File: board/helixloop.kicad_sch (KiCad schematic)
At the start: 69 parts, among them J6 USB_C_Receptacle, J7 Conn_01x03_Pin, SW6 SW_Push, U10 QSPI Flash, U6 USBLC6-2P6, U7 RP2040, U9 RT9078, Y6 12MHz

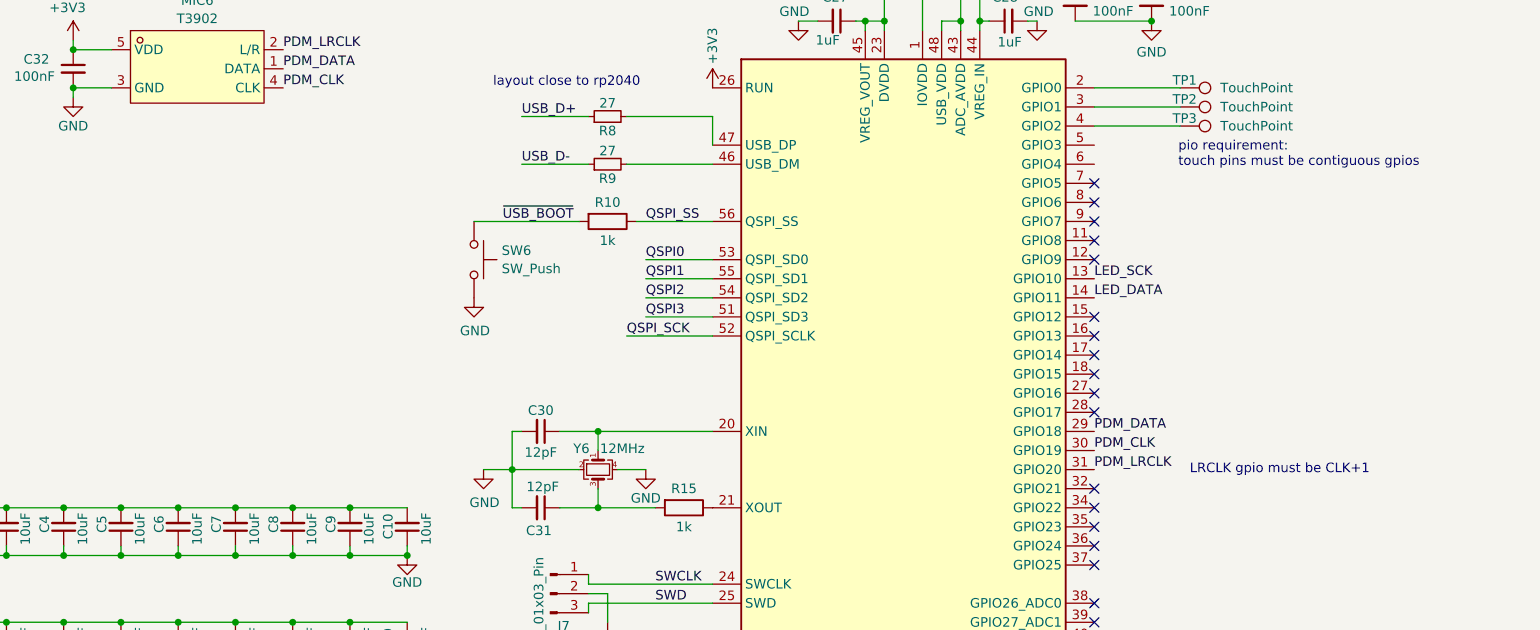
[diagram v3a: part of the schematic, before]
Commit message: add 3 touch points
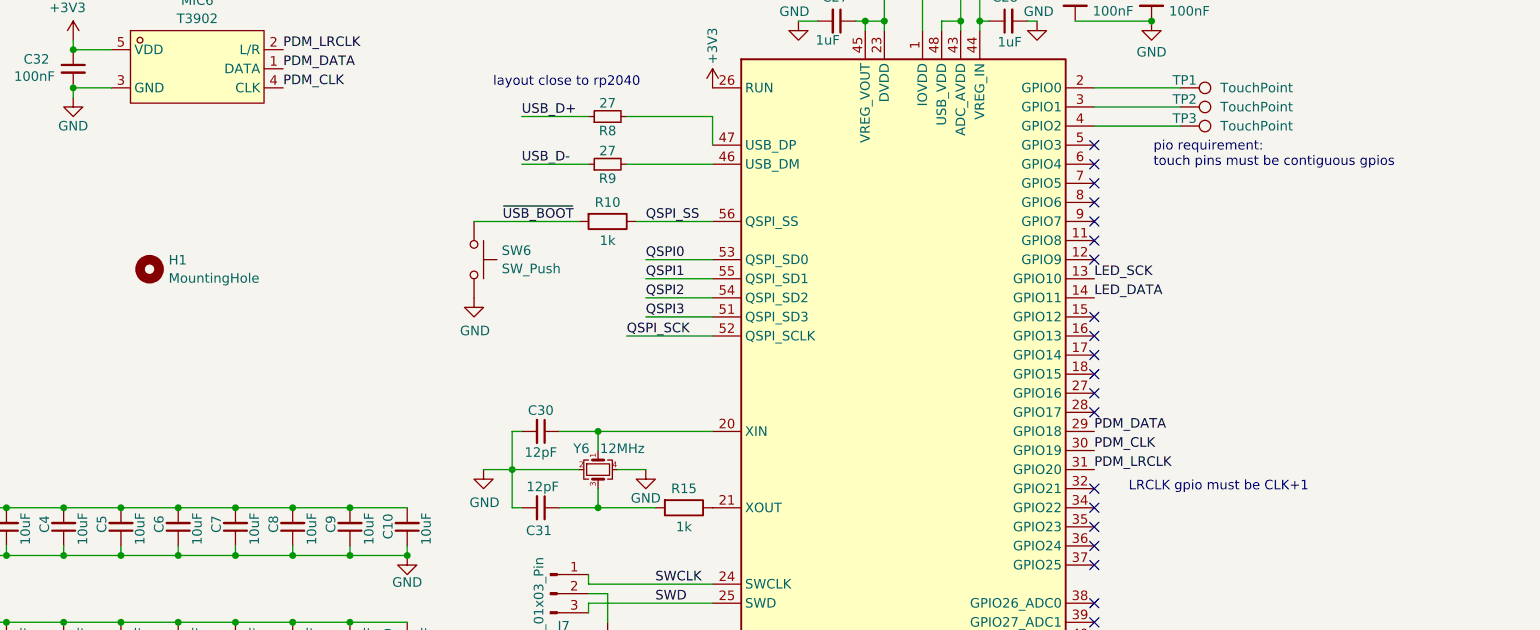
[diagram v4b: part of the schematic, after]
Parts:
- added H1: MountingHole, MountingHole:MountingHole_2.5mm, symbol Mechanical:MountingHole
- TP1: renamed from TP3; footprint TestPoint:TestPoint_Pad_D2.5mm -> helixloop:TouchPoint
- TP2: renamed from TP1; footprint TestPoint:TestPoint_Pad_D2.5mm -> helixloop:TouchPoint
- TP3: renamed from TP2; footprint TestPoint:TestPoint_Pad_D2.5mm -> helixloop:TouchPoint
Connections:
- net at TP1.1: now also U7.2 (GPIO0); no longer U7.4 (GPIO2)
- net at TP2.1: now also U7.3 (GPIO1); no longer U7.2 (GPIO0)
- net at TP3.1: now also U7.4 (GPIO2); no longer U7.3 (GPIO1)
- no-connect marks 32 -> 34
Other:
- moved on the sheet: TP1, TP2, TP3
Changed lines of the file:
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@@
 	)
 	(no_connect
+		(at 224.79 54.61)
+	)
+	(no_connect
 		(at 43.18 68.58)
 	)
@@
 	)
 	(no_connect
+		(at 224.79 52.07)
+	)
+	(no_connect
 		(at 224.79 77.47)
 	)
@@
 	(text "pio requirement:\ntouch pins must be contiguous gpios"
 		(exclude_from_sim no)
-		(at 235.966 53.34 0)
+		(at 232.664 53.34 0)
 		(effects
 			(font
@@
 	(text "LRCLK gpio must be CLK+1"
 		(exclude_from_sim no)
-		(at 237.49 95.25 0)
+		(at 229.362 97.536 0)
 		(effects
 			(font
@@
 	)
 	(symbol
+		(lib_id "Mechanical:MountingHole")
+		(at 99.06 68.58 0)
+		(unit 1)
+		(exclude_from_sim yes)
+		(in_bom no)
+		(on_board yes)
+		(dnp no)
+		(fields_autoplaced yes)
+		(property "Reference" "H1"
+			(at 101.6 67.3678 0)
+			(effects
+				(font
+					(size 1.27 1.27)
+				)
+				(justify left)
+			)
+		)
+		(property "Value" "MountingHole"
+			(at 101.6 69.7921 0)
+			(effects
+				(font
+					(size 1.27 1.27)
+				)
+				(justify left)
+			)
+		)
+		(property "Footprint" "MountingHole:MountingHole_2.5mm"
+			(at 99.06 68.58 0)
+			(effects
+				(font
+					(size 1.27 1.27)
+				)
+				(hide yes)
+			)
+		)
+		(property "Datasheet" "~"
+			(at 99.06 68.58 0)
+			(effects
+				(font
+					(size 1.27 1.27)
+				)
+				(hide yes)
+			)
+		)
+		(property "Description" "Mounting Hole without connection"
+			(at 99.06 68.58 0)
+			(effects
+				(font
+					(size 1.27 1.27)
+				)
+				(hide yes)
+			)
+		)
+		(property "Designation" ""
+			(at 99.06 68.58 0)
+			(effects
+				(font
+					(size 1.27 1.27)
+				)
+				(hide yes)
+			)
+		)
+		(instances
+			(project ""
+				(path "/1f30b1ea-44f0-467a-8ed8-643be513058b"
+					(reference "H1")
+					(unit 1)
+				)
+			)
+		)
+	)
+	(symbol
 		(lib_id "helixloop:QSPI Flash")
 		(at 241.3 152.4 0)
@@
 	(symbol
 		(lib_id "Connector:TestPoint")
-		(at 236.22 49.53 270)
+		(at 236.22 44.45 270)
 		(unit 1)
 		(exclude_from_sim no)
@@
 		(on_board yes)
 		(dnp no)
-		(property "Reference" "TP3"
-			(at 235.204 48.514 90)
+		(property "Reference" "TP1"
+			(at 235.204 43.434 90)
 			(effects
 				(font
@@
 		)
 		(property "Value" "TouchPoint"
-			(at 241.554 49.53 90)
+			(at 241.554 44.45 90)
 			(effects
 				(font
@@
 			)
 		)
-		(property "Footprint" "TestPoint:TestPoint_Pad_D2.5mm"
-			(at 236.22 54.61 0)
+		(property "Footprint" "helixloop:TouchPoint"
+			(at 236.22 49.53 0)
 			(effects
 				(font
@@
 		)
 		(property "Datasheet" "~"
-			(at 236.22 54.61 0)
+			(at 236.22 49.53 0)
 			(effects
 				(font
@@
 		)
 		(property "Description" "test point"
-			(at 236.22 49.53 0)
+			(at 236.22 44.45 0)
 			(effects
 				(font
@@
 		)
 		(property "Designation" ""
-			(at 236.22 49.53 0)
+			(at 236.22 44.45 0)
 			(effects
 				(font
@@
 			(project "helixloop"
 				(path "/1f30b1ea-44f0-467a-8ed8-643be513058b"
-					(reference "TP3")
+					(reference "TP1")
 					(unit 1)
 				)
@@
 	(symbol
 		(lib_id "Connector:TestPoint")
-		(at 236.22 46.99 270)
+		(at 236.22 49.53 270)
 		(unit 1)
 		(exclude_from_sim no)
@@
 		(on_board yes)
 		(dnp no)
-		(property "Reference" "TP2"
-			(at 235.204 45.974 90)
+		(property "Reference" "TP3"
+			(at 235.204 48.514 90)
 			(effects
 				(font
@@
 		)
 		(property "Value" "TouchPoint"
-			(at 241.554 46.99 90)
+			(at 241.554 49.53 90)
 			(effects
 				(font
@@
 			)
 		)
-		(property "Footprint" "TestPoint:TestPoint_Pad_D2.5mm"
-			(at 236.22 52.07 0)
+		(property "Footprint" "helixloop:TouchPoint"
+			(at 236.22 54.61 0)
 			(effects
 				(font
@@
 		)
 		(property "Datasheet" "~"
-			(at 236.22 52.07 0)
+			(at 236.22 54.61 0)
 			(effects
 				(font
@@
 		)
 		(property "Description" "test point"
-			(at 236.22 46.99 0)
+			(at 236.22 49.53 0)
 			(effects
 				(font
@@
 		)
 		(property "Designation" ""
-			(at 236.22 46.99 0)
+			(at 236.22 49.53 0)
 			(effects
 				(font
@@
 			(project "helixloop"
 				(path "/1f30b1ea-44f0-467a-8ed8-643be513058b"
-					(reference "TP2")
+					(reference "TP3")
 					(unit 1)
 				)
@@
 	(symbol
 		(lib_id "Connector:TestPoint")
-		(at 236.22 44.45 270)
+		(at 236.22 46.99 270)
 		(unit 1)
 		(exclude_from_sim no)
@@
 		(on_board yes)
 		(dnp no)
-		(property "Reference" "TP1"
-			(at 235.204 43.434 90)
+		(property "Reference" "TP2"
+			(at 235.204 45.974 90)
 			(effects
 				(font
@@
 		)
 		(property "Value" "TouchPoint"
-			(at 241.554 44.45 90)
+			(at 241.554 46.99 90)
 			(effects
 				(font
@@
 			)
 		)
-		(property "Footprint" "TestPoint:TestPoint_Pad_D2.5mm"
-			(at 236.22 49.53 0)
+		(property "Footprint" "helixloop:TouchPoint"
+			(at 236.22 52.07 0)
 			(effects
 				(font
@@
 		)
 		(property "Datasheet" "~"
-			(at 236.22 49.53 0)
+			(at 236.22 52.07 0)
 			(effects
 				(font
@@
 		)
 		(property "Description" "test point"
-			(at 236.22 44.45 0)
+			(at 236.22 46.99 0)
 			(effects
 				(font
@@
 		)
 		(property "Designation" ""
-			(at 236.22 44.45 0)
+			(at 236.22 46.99 0)
 			(effects
 				(font
@@
 			(project "helixloop"
 				(path "/1f30b1ea-44f0-467a-8ed8-643be513058b"
-					(reference "TP1")
+					(reference "TP2")
 					(unit 1)
 				)

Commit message: add spiral drawing back in and remove homedir path; fix mic symbol link
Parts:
- MIC6: footprint easyeda2kicad:MIC-SMD_5P-L3.5-W2.7-TL_MMICT390200012 -> helixloop:KEY-SMD_L3.0-W2.5-LS4.0
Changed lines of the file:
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@@
 			)
 		)
-		(property "Footprint" "easyeda2kicad:MIC-SMD_5P-L3.5-W2.7-TL_MMICT390200012"
+		(property "Footprint" "helixloop:KEY-SMD_L3.0-W2.5-LS4.0"
 			(at 105.156 51.816 0)
 			(effects

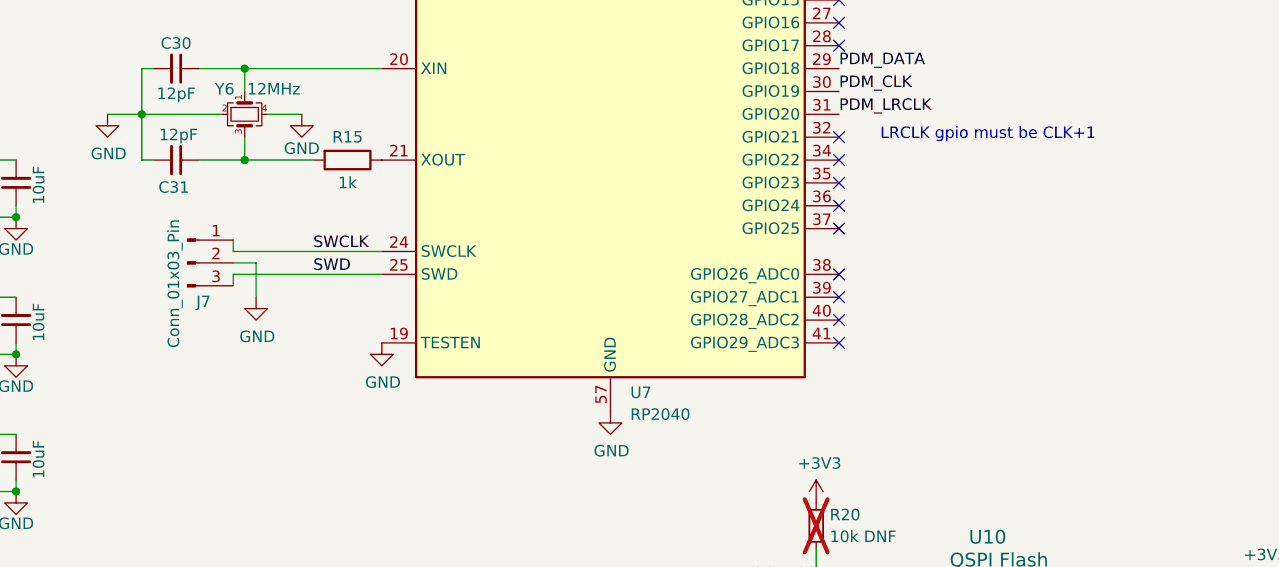
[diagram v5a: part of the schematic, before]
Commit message: export swd pins and all four analog pins to small tht connectors; tweak back-copper gnd fill margins
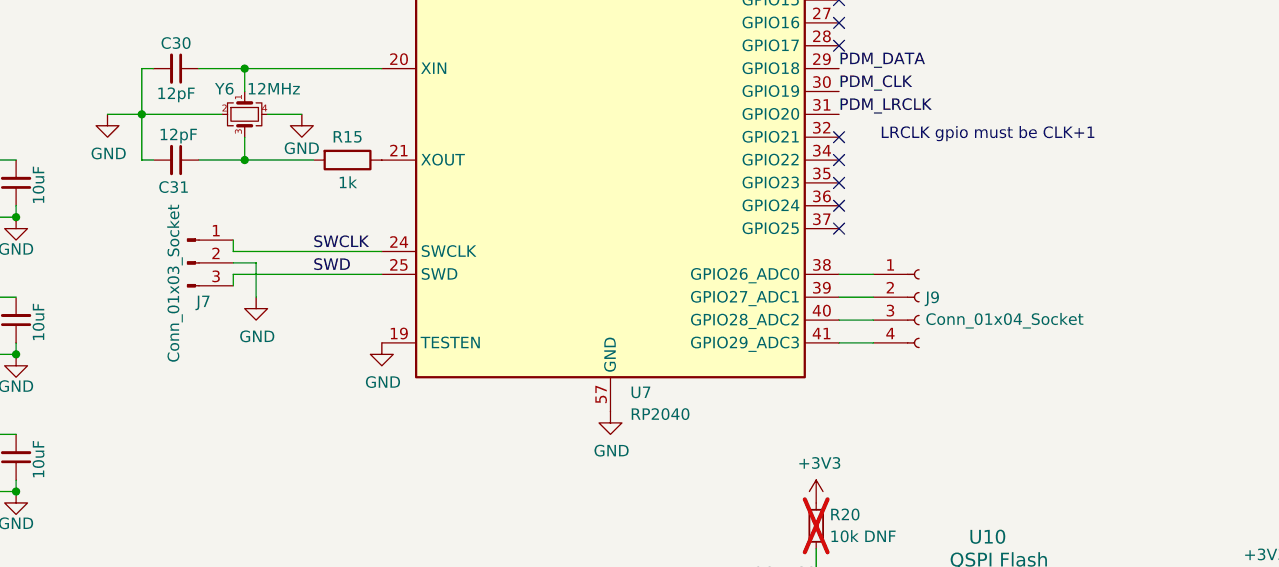
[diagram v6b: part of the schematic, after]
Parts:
- added J9: Conn_01x04_Socket, helixloop:MinimalPinSocket_1x04_P1.27mm_Vertical, symbol Connector:Conn_01x04_Socket
- J7: value Conn_01x03_Pin -> Conn_01x03_Socket; footprint penta:SMD_Pad_01x03_1.27mm -> helixloop:MinimalPinSocket_1x03_P1.27mm_Vertical
- MIC6: footprint helixloop:KEY-SMD_L3.0-W2.5-LS4.0 -> helixloop:MIC_T3902
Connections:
- net at U7.38 (GPIO26_ADC0): now also J9.1 (Pin_1)
- net at U7.39 (GPIO27_ADC1): now also J9.2 (Pin_2)
- net at U7.40 (GPIO28_ADC2): now also J9.3 (Pin_3)
- net at U7.41 (GPIO29_ADC3): now also J9.4 (Pin_4)
- no-connect marks 34 -> 30
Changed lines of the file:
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@@
 	)
 	(no_connect
-		(at 224.79 113.03)
-	)
-	(no_connect
 		(at 224.79 85.09)
 	)
@@
 	)
 	(no_connect
-		(at 224.79 120.65)
-	)
-	(no_connect
 		(at 224.79 97.79)
 	)
@@
 	)
 	(no_connect
-		(at 224.79 115.57)
-	)
-	(no_connect
 		(at 43.18 53.34)
 	)
@@
 	)
 	(no_connect
-		(at 224.79 118.11)
-	)
-	(no_connect
 		(at 224.79 67.31)
 	)
@@
 	(wire
 		(pts
+			(xy 224.79 118.11) (xy 228.6 118.11)
+		)
+		(stroke
+			(width 0)
+			(type default)
+		)
+	)
+	(wire
+		(pts
 			(xy 201.93 22.86) (xy 209.55 22.86)
 		)
@@
 	(wire
 		(pts
+			(xy 224.79 120.65) (xy 228.6 120.65)
+		)
+		(stroke
+			(width 0)
+			(type default)
+		)
+	)
+	(wire
+		(pts
 			(xy 133.35 106.68) (xy 133.35 105.41)
 		)
@@
 	(wire
 		(pts
+			(xy 224.79 113.03) (xy 228.6 113.03)
+		)
+		(stroke
+			(width 0)
+			(type default)
+		)
+	)
+	(wire
+		(pts
 			(xy 118.11 121.92) (xy 110.49 121.92)
 		)
@@
 	(wire
 		(pts
+			(xy 224.79 115.57) (xy 228.6 115.57)
+		)
+		(stroke
+			(width 0)
+			(type default)
+		)
+	)
+	(wire
+		(pts
 			(xy 74.93 168.91) (xy 77.47 168.91)
 		)
@@
 			)
 		)
-		(property "Footprint" "helixloop:KEY-SMD_L3.0-W2.5-LS4.0"
+		(property "Footprint" "helixloop:MIC_T3902"
 			(at 105.156 51.816 0)
 			(effects
@@
 			)
 		)
-		(property "Value" "Conn_01x03_Pin"
+		(property "Value" "Conn_01x03_Socket"
 			(at 150.876 114.046 90)
 			(effects
@@
 			)
 		)
-		(property "Footprint" "penta:SMD_Pad_01x03_1.27mm"
+		(property "Footprint" "helixloop:MinimalPinSocket_1x03_P1.27mm_Vertical"
 			(at 152.4 111.76 0)
 			(effects
@@
 					(unit 1)
 				)
+			)
+		)
+	)
+	(symbol
+		(lib_id "Connector:Conn_01x04_Socket")
+		(at 233.68 115.57 0)
+		(unit 1)
+		(exclude_from_sim no)
+		(in_bom no)
+		(on_board yes)
+		(dnp no)
+		(fields_autoplaced yes)
+		(property "Reference" "J9"
+			(at 234.3912 115.6278 0)
+			(effects
+				(font
+					(size 1.27 1.27)
+				)
+				(justify left)
+			)
+		)
+		(property "Value" "Conn_01x04_Socket"
+			(at 234.3912 118.0521 0)
+			(effects
+				(font
+					(size 1.27 1.27)
+				)
+				(justify left)
+			)
+		)
+		(property "Footprint" "helixloop:MinimalPinSocket_1x04_P1.27mm_Vertical"
+			(at 233.68 115.57 0)
+			(effects
+				(font
+					(size 1.27 1.27)
+				)
+				(hide yes)
+			)
+		)
+		(property "Datasheet" "~"
+			(at 233.68 115.57 0)
+			(effects
+				(font
+					(size 1.27 1.27)
+				)
+				(hide yes)
+			)
+		)
+		(property "Description" "Generic connector, single row, 01x04, script generated"
+			(at 233.68 115.57 0)
+			(effects
+				(font
+					(size 1.27 1.27)
+				)
+				(hide yes)
+			)
+		)
+		(property "Designation" ""
+			(at 233.68 115.57 0)
+			(effects
+				(font
+					(size 1.27 1.27)
+				)
+				(hide yes)
+			)
+		)
+		(pin "2"
+		)
+		(pin "4"
+		)
+		(pin "3"
+		)
+		(pin "1"
+		)
+		(instances
+			(project ""
+				(path "/1f30b1ea-44f0-467a-8ed8-643be513058b"
+					(reference "J9")
+					(unit 1)
+				)

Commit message: add more mounting holes
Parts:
- removed H1: MountingHole, MountingHole:MountingHole_2.5mm, symbol Mechanical:MountingHole
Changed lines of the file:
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@@
-	)
-	(symbol
-		(lib_id "Mechanical:MountingHole")
-		(at 99.06 68.58 0)
-		(unit 1)
-		(exclude_from_sim yes)
-		(in_bom no)
-		(on_board yes)
-		(dnp no)
-		(fields_autoplaced yes)
-		(property "Reference" "H1"
-			(at 101.6 67.3678 0)
-			(effects
-				(font
-					(size 1.27 1.27)
-				)
-				(justify left)
-			)
-		)
-		(property "Value" "MountingHole"
-			(at 101.6 69.7921 0)
-			(effects
-				(font
-					(size 1.27 1.27)
-				)
-				(justify left)
-			)
-		)
-		(property "Footprint" "MountingHole:MountingHole_2.5mm"
-			(at 99.06 68.58 0)
-			(effects
-				(font
-					(size 1.27 1.27)
-				)
-				(hide yes)
-			)
-		)
-		(property "Datasheet" "~"
-			(at 99.06 68.58 0)
-			(effects
-				(font
-					(size 1.27 1.27)
-				)
-				(hide yes)
-			)
-		)
-		(property "Description" "Mounting Hole without connection"
-			(at 99.06 68.58 0)
-			(effects
-				(font
-					(size 1.27 1.27)
-				)
-				(hide yes)
-			)
-		)
-		(property "Designation" ""
-			(at 99.06 68.58 0)
-			(effects
-				(font
-					(size 1.27 1.27)
-				)
-				(hide yes)
-			)
-		)
-		(instances
-			(project ""
-				(path "/1f30b1ea-44f0-467a-8ed8-643be513058b"
-					(reference "H1")
-					(unit 1)
-				)
-			)
-		)
 	)
 	(symbol
